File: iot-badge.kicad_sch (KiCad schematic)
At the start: 28 parts, among them J1 USB_C_Receptacle_USB2.0, Q1 BC847, Q2 BC847, SW1 SW_Push, SW2 SW_Push, SW3 SW_Push, SW4 SW_Push, SW5 SW_Push, SW6 SW_Push, U1 ESP32-WROOM-32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

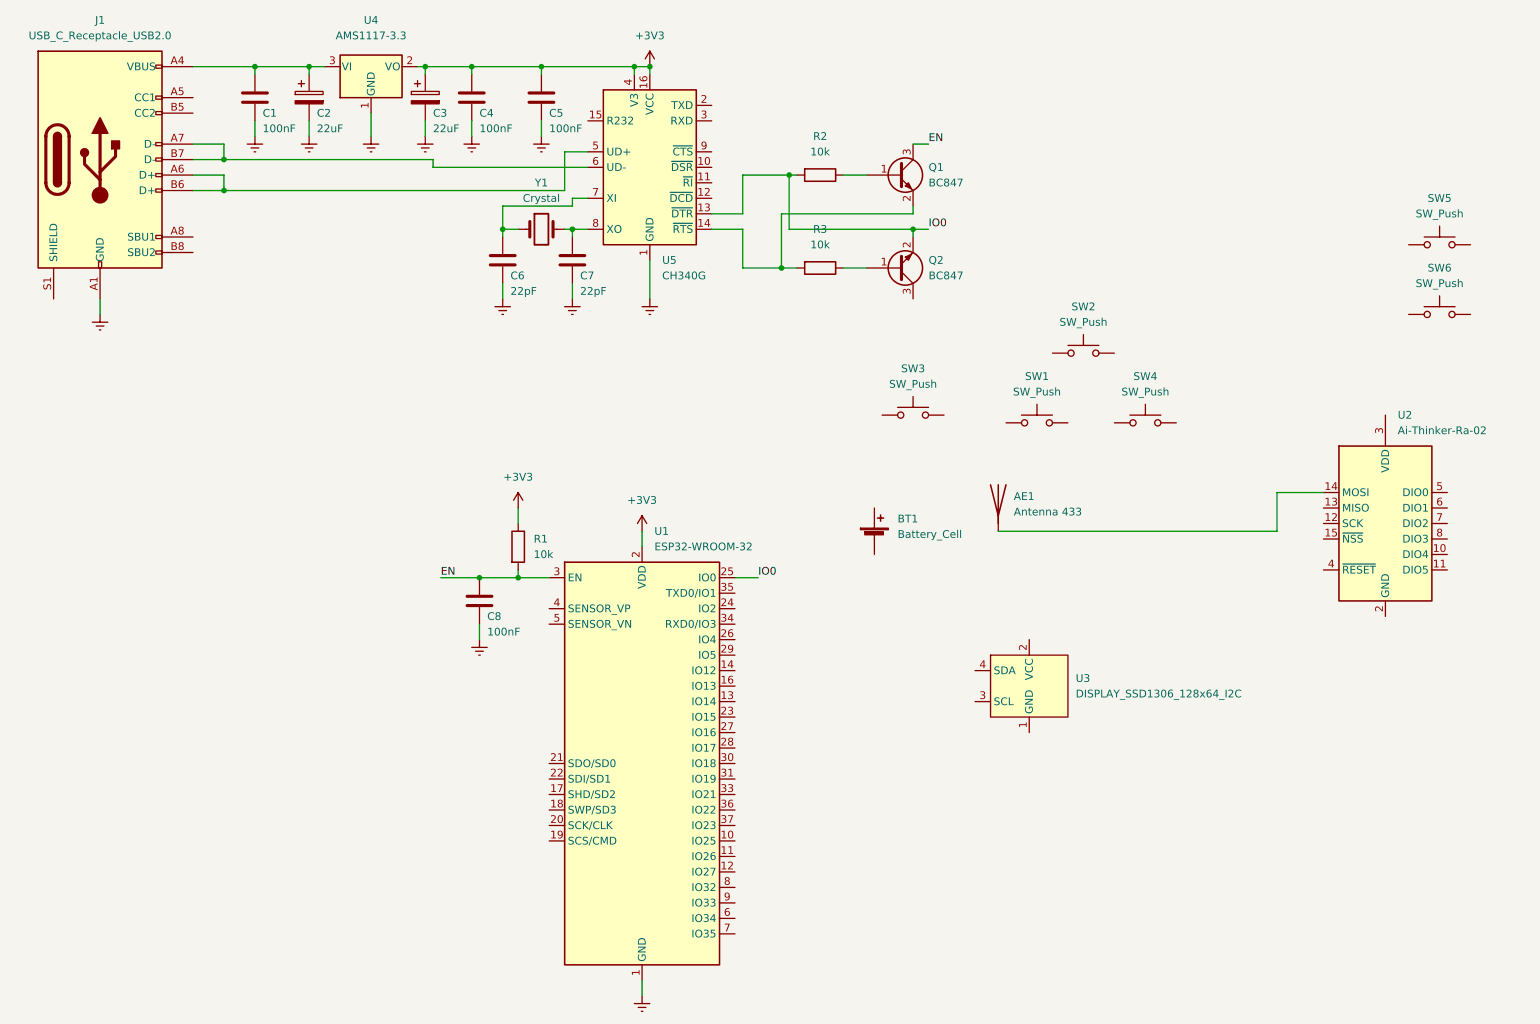
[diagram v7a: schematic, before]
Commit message: ant needs routing rules
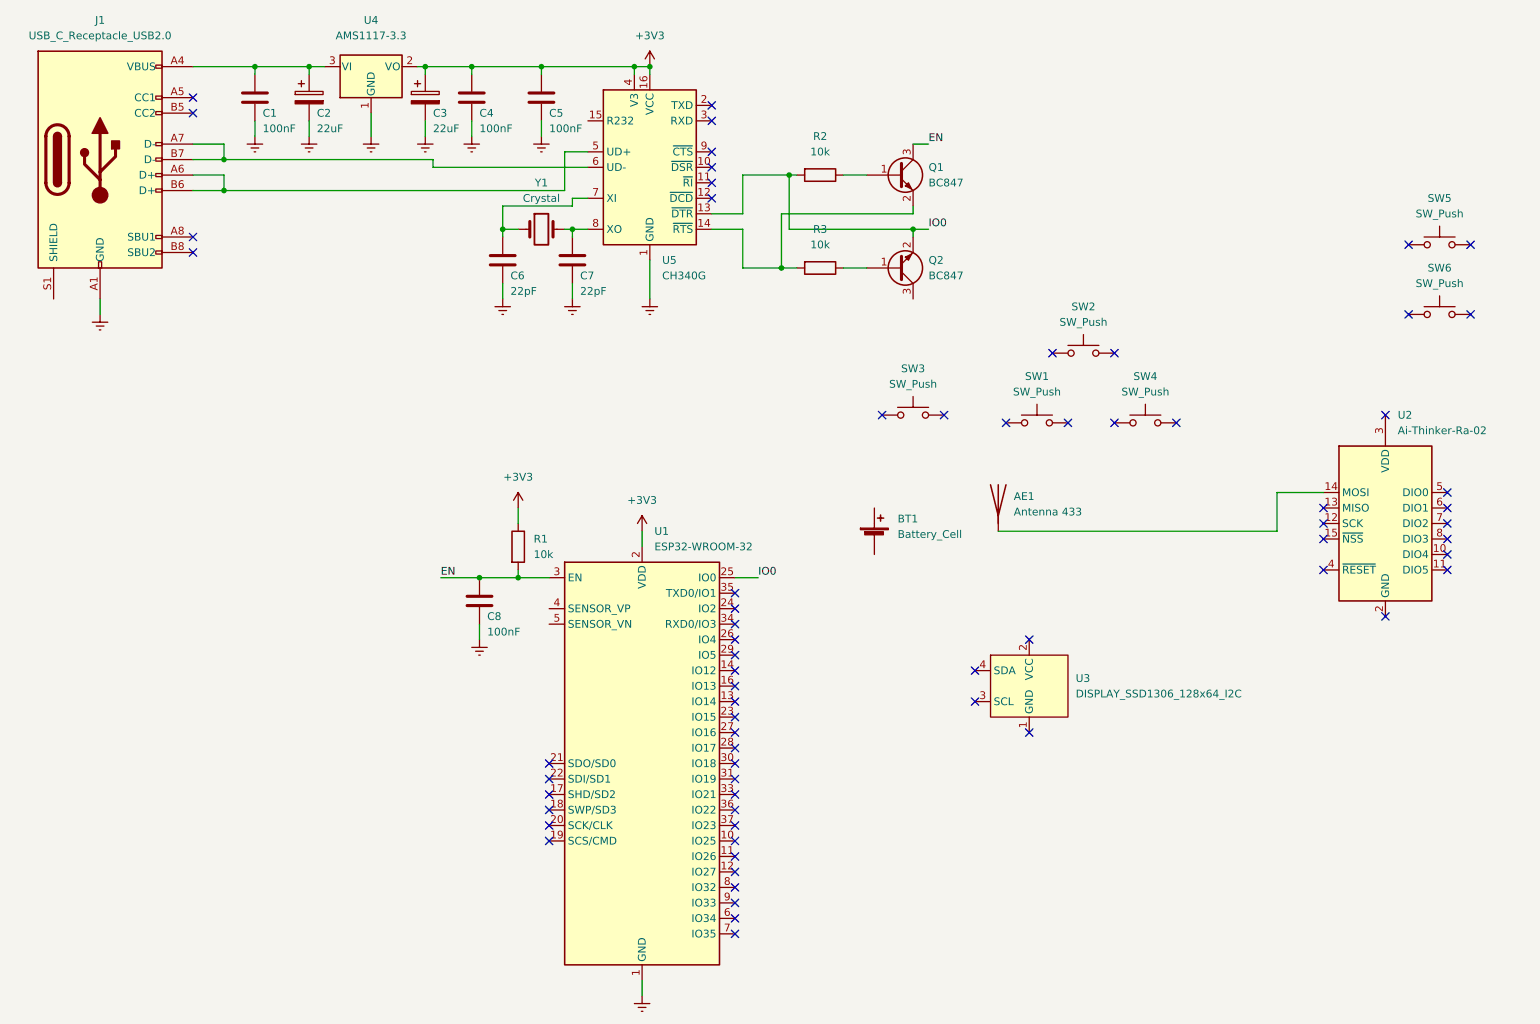
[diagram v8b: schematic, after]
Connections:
- no-connect marks 0 -> 67
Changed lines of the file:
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@@
   (junction (at 102.87 59.69) (diameter 0) (color 0 0 0 0)
   )
+  (no_connect (at 251.46 62.23))
+  (no_connect (at 110.49 147.32))
+  (no_connect (at 140.97 154.94))
+  (no_connect (at 247.65 123.19))
+  (no_connect (at 257.81 110.49))
+  (no_connect (at 137.16 41.91))
+  (no_connect (at 251.46 73.66))
+  (no_connect (at 137.16 52.07))
+  (no_connect (at 213.36 91.44))
+  (no_connect (at 195.58 91.44))
+  (no_connect (at 140.97 119.38))
+  (no_connect (at 140.97 121.92))
+  (no_connect (at 257.81 107.95))
+  (no_connect (at 257.81 113.03))
+  (no_connect (at 140.97 147.32))
+  (no_connect (at 140.97 175.26))
+  (no_connect (at 203.2 91.44))
+  (no_connect (at 257.81 102.87))
+  (no_connect (at 110.49 157.48))
+  (no_connect (at 140.97 144.78))
+  (no_connect (at 140.97 172.72))
+  (no_connect (at 257.81 105.41))
+  (no_connect (at 137.16 39.37))
+  (no_connect (at 140.97 167.64))
+  (no_connect (at 180.34 132.08))
+  (no_connect (at 137.16 46.99))
+  (no_connect (at 52.07 60.96))
+  (no_connect (at 140.97 165.1))
+  (no_connect (at 261.62 73.66))
+  (no_connect (at 237.49 115.57))
+  (no_connect (at 110.49 152.4))
+  (no_connect (at 110.49 149.86))
+  (no_connect (at 140.97 129.54))
+  (no_connect (at 237.49 105.41))
+  (no_connect (at 140.97 149.86))
+  (no_connect (at 140.97 142.24))
+  (no_connect (at 110.49 160.02))
+  (no_connect (at 140.97 139.7))
+  (no_connect (at 137.16 49.53))
+  (no_connect (at 137.16 54.61))
+  (no_connect (at 257.81 115.57))
+  (no_connect (at 247.65 90.17))
+  (no_connect (at 140.97 160.02))
+  (no_connect (at 189.23 142.24))
+  (no_connect (at 140.97 157.48))
+  (no_connect (at 140.97 137.16))
+  (no_connect (at 110.49 154.94))
+  (no_connect (at 180.34 137.16))
+  (no_connect (at 189.23 127))
+  (no_connect (at 185.42 91.44))
+  (no_connect (at 237.49 110.49))
+  (no_connect (at 52.07 38.1))
+  (no_connect (at 140.97 170.18))
+  (no_connect (at 140.97 127))
+  (no_connect (at 237.49 107.95))
+  (no_connect (at 165.1 90.17))
+  (no_connect (at 140.97 134.62))
+  (no_connect (at 193.04 80.01))
+  (no_connect (at 140.97 132.08))
+  (no_connect (at 140.97 124.46))
+  (no_connect (at 52.07 63.5))
+  (no_connect (at 140.97 152.4))
+  (no_connect (at 140.97 162.56))
+  (no_connect (at 203.2 80.01))
+  (no_connect (at 175.26 90.17))
+  (no_connect (at 261.62 62.23))
+  (no_connect (at 52.07 40.64))
   (wire (pts (xy 91.44 49.53) (xy 91.44 48.26))
     (stroke (width 0) (type default) (color 0 0 0 0))
